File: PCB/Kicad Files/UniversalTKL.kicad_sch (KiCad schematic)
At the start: 205 parts, among them J1 Reset Jumper, J2 CONN_RGB, J3 CONN_DB, J4 ISP_Breakout, U1 ATmega32U4-M, Y1 Resonator_Small

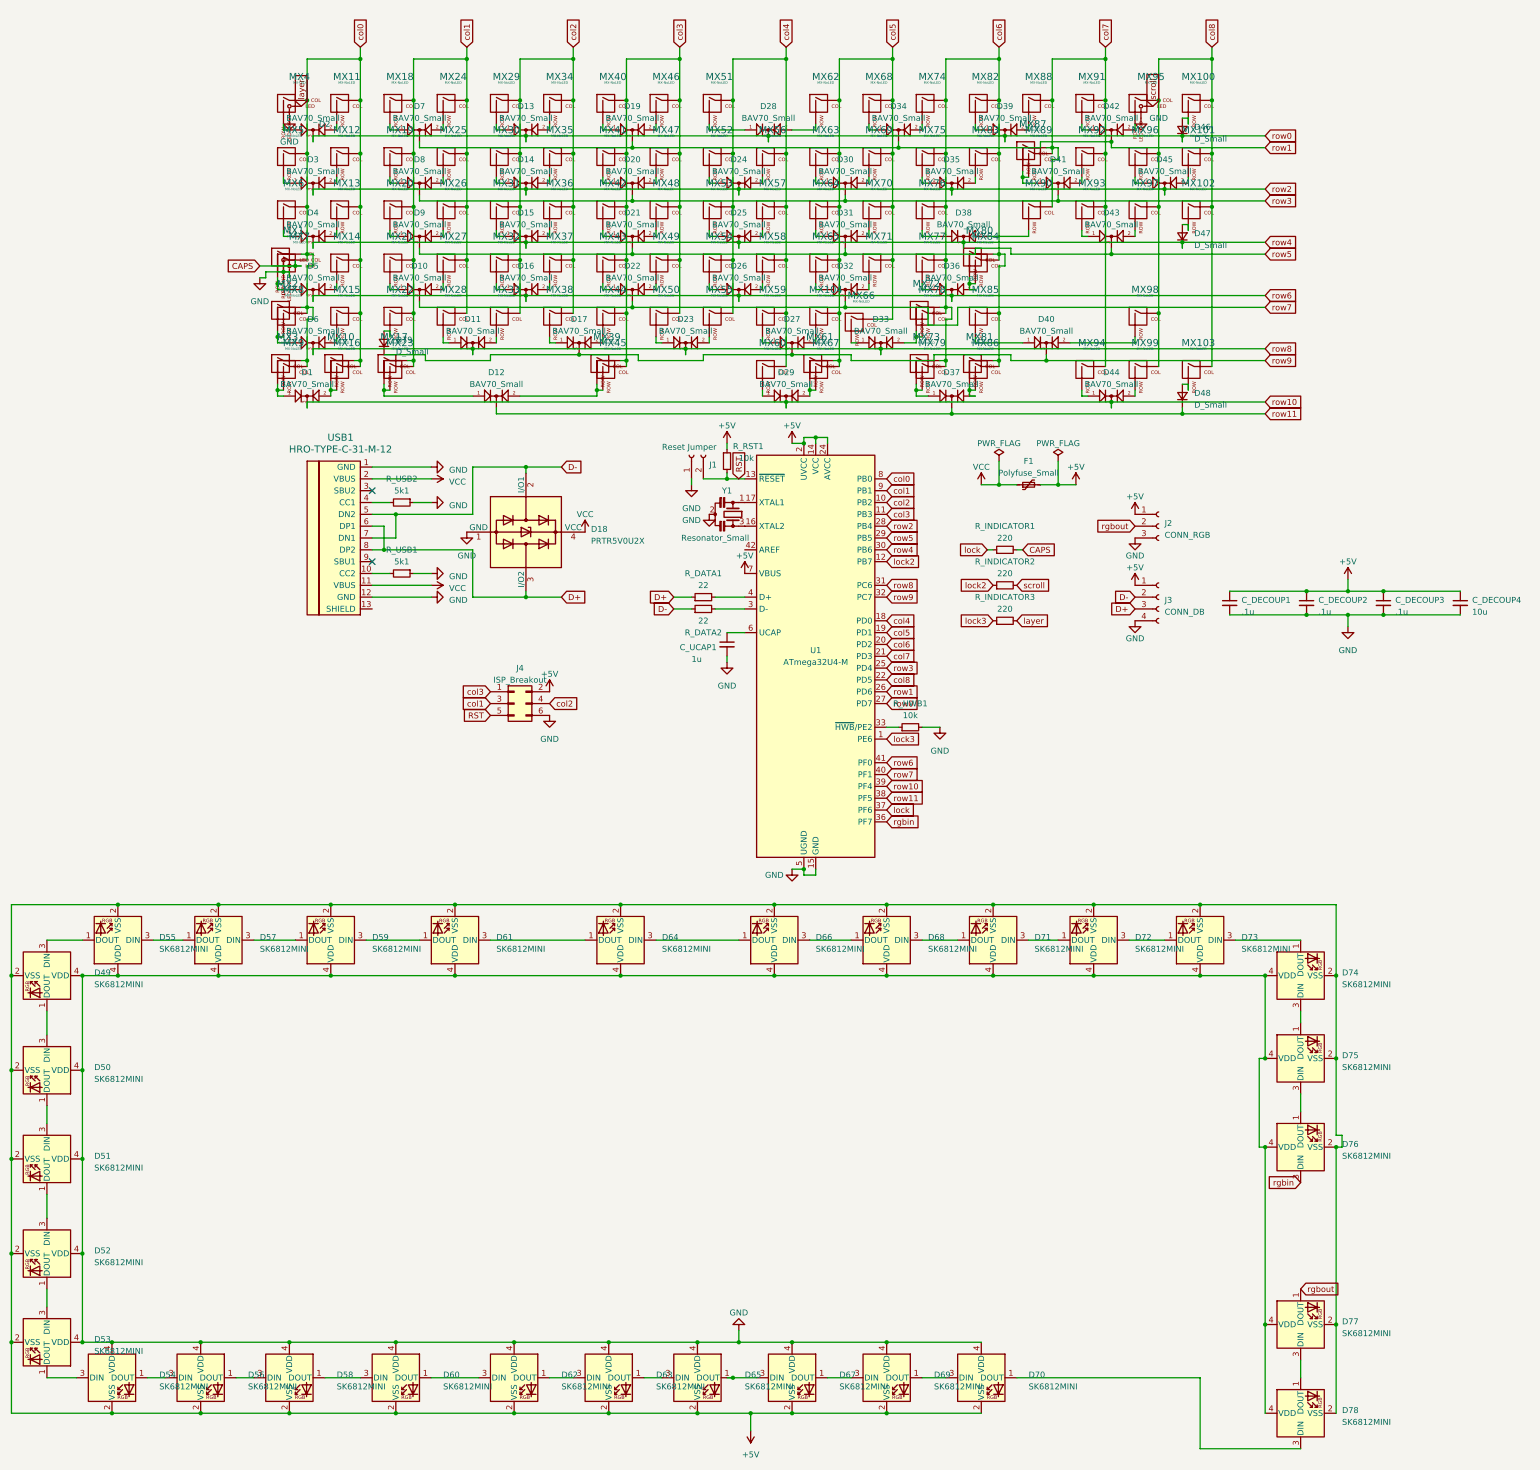
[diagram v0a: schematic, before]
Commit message: Fixed PCB, Changed to Support Jane Plate
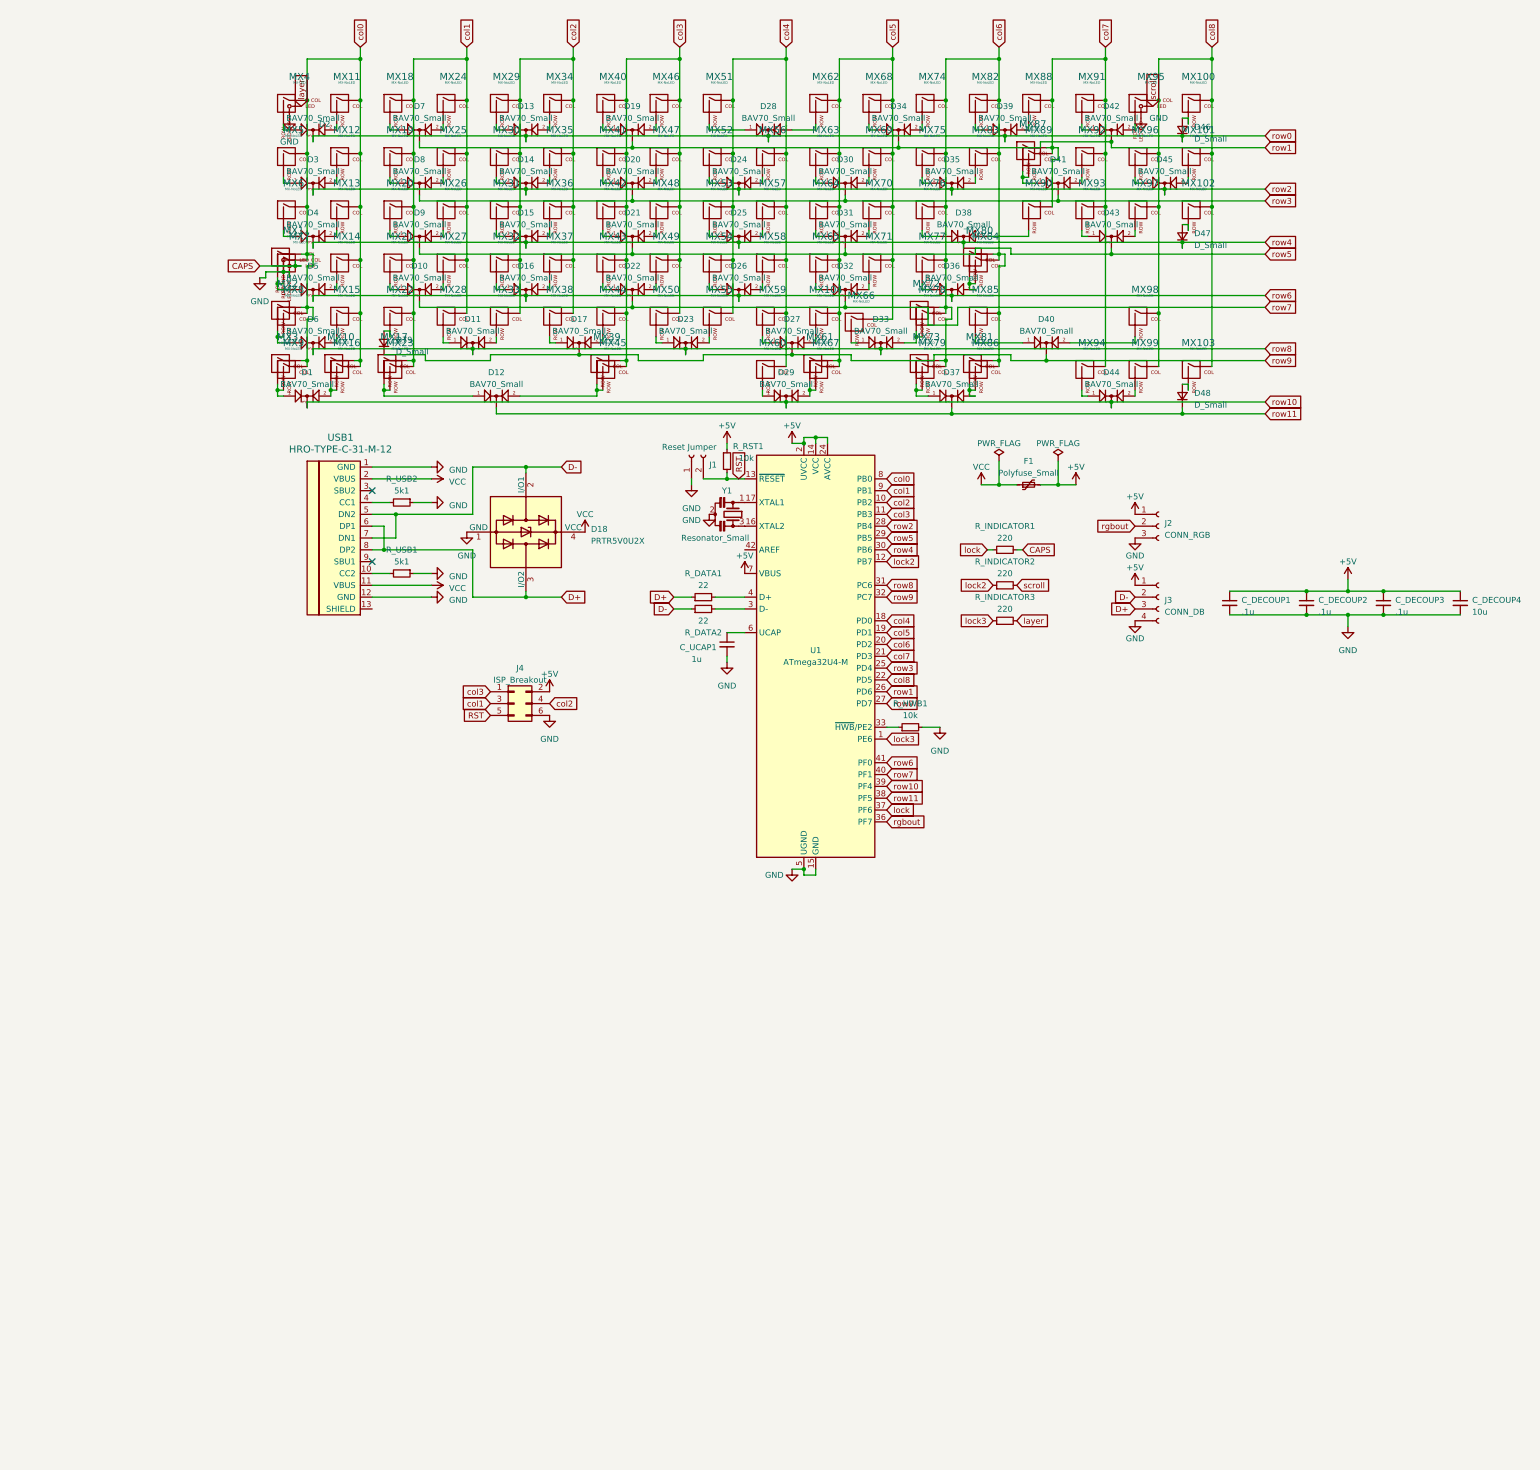
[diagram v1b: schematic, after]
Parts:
- removed D49, D50, D51, D52, D53, D54, D55, D56, D57, D58, D59, D60, D61, D62, D63, D64, D65, D66, D67, D68, D69, D70, D71, D72, D73, D74, D75, D76, D77, D78: SK6812MINI, LED_SMD:LED_SK6812MINI_PLCC4_3.5x3.5mm_P1.75mm, symbol LED:SK6812MINI
- MX1: footprint MX_Alps_Hybrid:MX-1.25U -> FancyHybridPrints:MX-1.25U
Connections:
- net rgbin is gone; now on net rgbout: U1.36 (PF7)
